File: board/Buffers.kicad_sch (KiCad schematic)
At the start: 14 parts, among them U12 74F86, U17 74F04, U52 74LS245, U53 74LS245, U54 74LS245, U55 74LS245, U56 74F541, U57 74F541

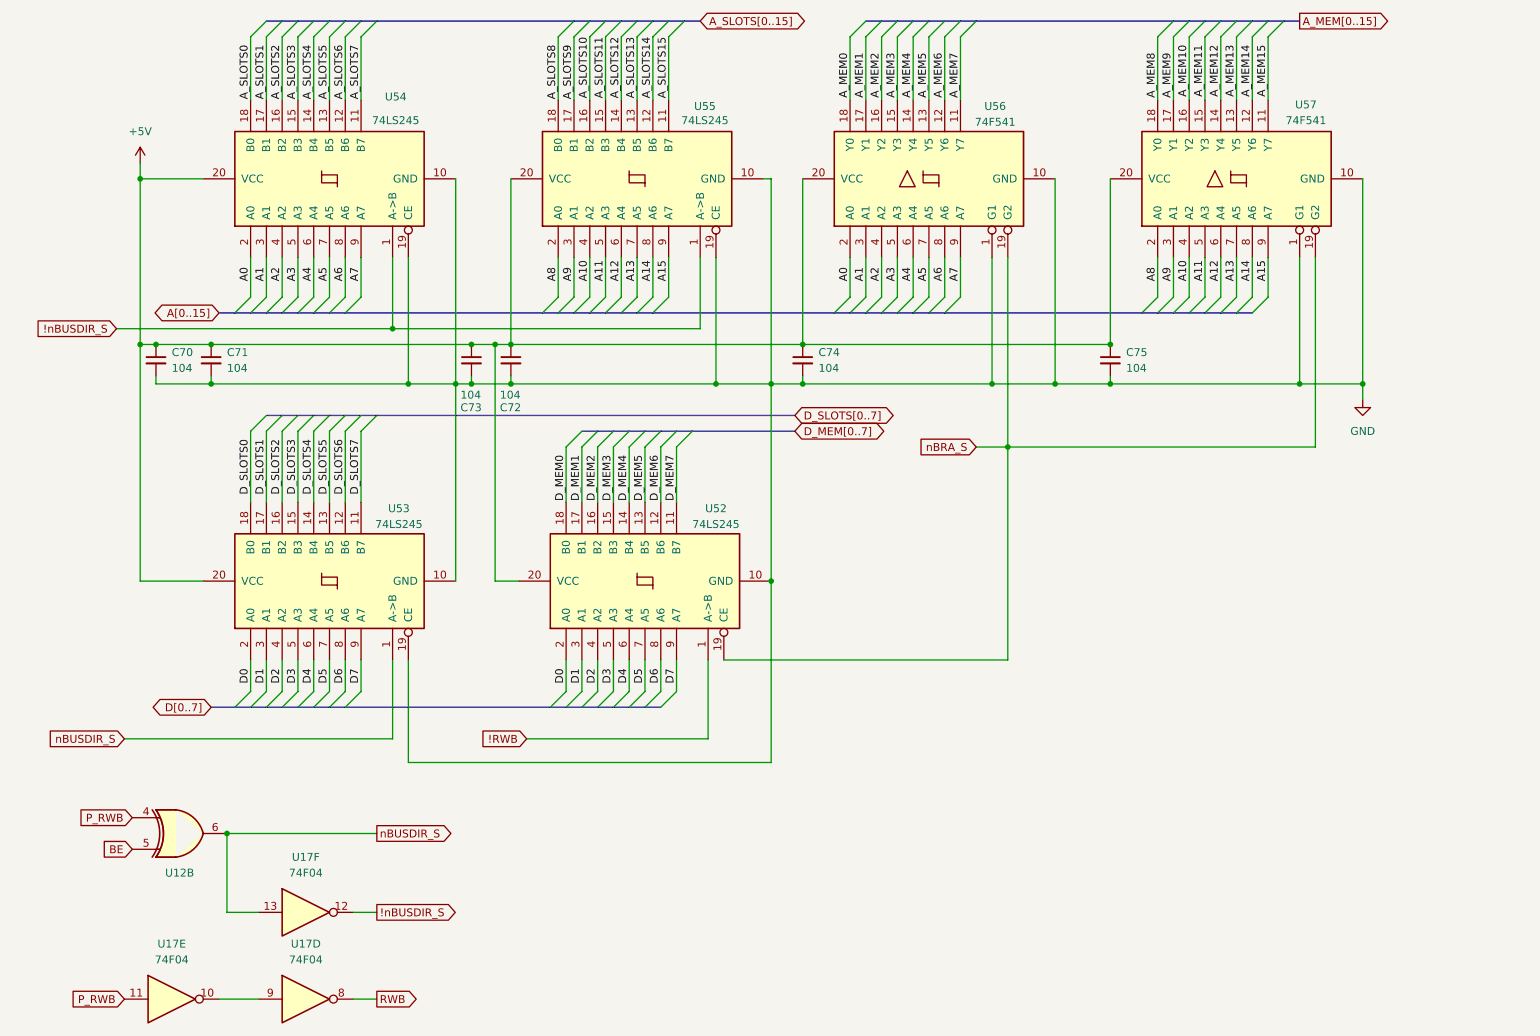
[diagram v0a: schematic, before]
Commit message: V1.3C without board traces
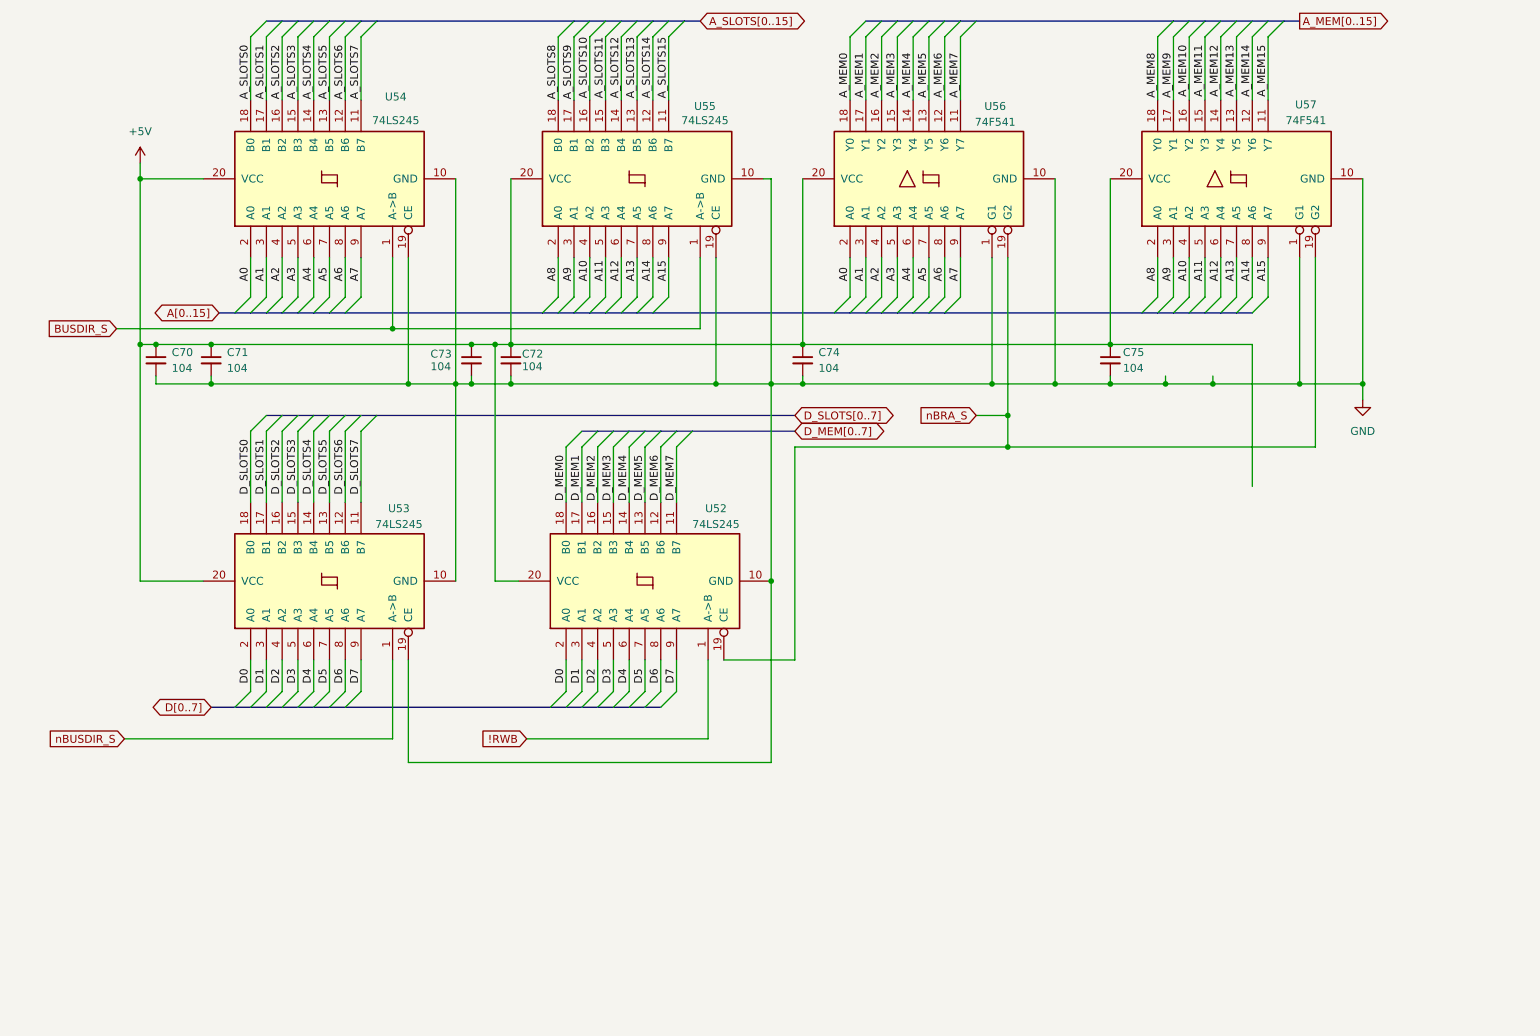
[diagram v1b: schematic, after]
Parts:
- removed U12: 74F86, Package_DIP:DIP-14_W7.62mm_Socket_LongPads, symbol 74xx:74LS86
- removed U17: 74F04, Package_DIP:DIP-14_W7.62mm_Socket_LongPads, symbol 74xx:74LS04
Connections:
- net !nBUSDIR_S renamed BUSDIR_S

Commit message: V1.4E
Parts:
- removed C72, C73, C75: 104, Capacitor_THT:C_Disc_D5.0mm_W2.5mm_P5.00mm, symbol Device:C_Small
- removed U53: 74LS245, Package_DIP:DIP-20_W7.62mm_Socket_LongPads, symbol 74xx:74LS245
- removed U56, U57: 74F541, Package_DIP:DIP-20_W7.62mm_Socket_LongPads, symbol 74xx:74LS541
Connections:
- net A_SLOTS0 is gone; now on net A0: U54.18 (B0)
- net A_SLOTS1 is gone; now on net A1: U54.17 (B1)
- net A_SLOTS10 is gone; now on net A10: U55.16 (B2)
- net A_SLOTS11 is gone; now on net A11: U55.15 (B3)
- net A_SLOTS12 is gone; now on net A12: U55.14 (B4)
- net A_SLOTS13 is gone; now on net A13: U55.13 (B5)
- net A_SLOTS14 is gone; now on net A14: U55.12 (B6)
- net A_SLOTS15 is gone; now on net A15: U55.11 (B7)
- net A_SLOTS2 is gone; now on net A2: U54.16 (B2)
- net A_SLOTS3 is gone; now on net A3: U54.15 (B3)
- net A_SLOTS4 is gone; now on net A4: U54.14 (B4)
- net A_SLOTS5 is gone; now on net A5: U54.13 (B5)
- net A_SLOTS6 is gone; now on net A6: U54.12 (B6)
- net A_SLOTS7 is gone; now on net A7: U54.11 (B7)
- net A_SLOTS8 is gone; now on net A8: U55.18 (B0)
- net A_SLOTS9 is gone; now on net A9: U55.17 (B1)
- net D_MEM0 is gone; now on net D0: U52.18 (B0)
- net D_MEM1 is gone; now on net D1: U52.17 (B1)
- net D_MEM2 is gone; now on net D2: U52.16 (B2)
- net D_MEM3 is gone; now on net D3: U52.15 (B3)
- net D_MEM4 is gone; now on net D4: U52.14 (B4)
- net D_MEM5 is gone; now on net D5: U52.13 (B5)
- net D_MEM6 is gone; now on net D6: U52.12 (B6)
- net D_MEM7 is gone; now on net D7: U52.11 (B7)
- net GND is gone; now on net nBRA_S: C70.2, C71.2, C74.2, U52.10 (GND), U54.10 (GND), U54.19 (CE), U55.10 (GND), U55.19 (CE)
- net A0: no longer U54.2 (A0)
- net A1: no longer U54.3 (A1)
- net A10: no longer U55.4 (A2)
- net A11: no longer U55.5 (A3)
- net A12: no longer U55.6 (A4)
- net A13: no longer U55.7 (A5)
- net A14: no longer U55.8 (A6)
- net A15: no longer U55.9 (A7)
- net A2: no longer U54.4 (A2)
- net A3: no longer U54.5 (A3)
- net A4: no longer U54.6 (A4)
- net A5: no longer U54.7 (A5)
- net A6: no longer U54.8 (A6)
- net A7: no longer U54.9 (A7)
- net A8: no longer U55.2 (A0)
- net A9: no longer U55.3 (A1)
- net D0: no longer U52.2 (A0)
- net D1: no longer U52.3 (A1)
- net D2: no longer U52.4 (A2)
- net D3: no longer U52.5 (A3)
- net D4: no longer U52.6 (A4)
- net D5: no longer U52.7 (A5)
- net D6: no longer U52.8 (A6)
- net D7: no longer U52.9 (A7)
- new net PA0: U54.2 (A0)
- new net PA1: U54.3 (A1)
- new net PA10: U55.4 (A2)
- new net PA11: U55.5 (A3)
- new net PA12: U55.6 (A4)
- new net PA13: U55.7 (A5)
- new net PA14: U55.8 (A6)
- new net PA15: U55.9 (A7)
- new net PA2: U54.4 (A2)
- new net PA3: U54.5 (A3)
- new net PA4: U54.6 (A4)
- new net PA5: U54.7 (A5)
- new net PA6: U54.8 (A6)
- new net PA7: U54.9 (A7)
- new net PA8: U55.2 (A0)
- new net PA9: U55.3 (A1)
- new net PD0: U52.2 (A0)
- new net PD1: U52.3 (A1)
- new net PD2: U52.4 (A2)
- new net PD3: U52.5 (A3)
- new net PD4: U52.6 (A4)
- new net PD5: U52.7 (A5)
- new net PD6: U52.8 (A6)
- new net PD7: U52.9 (A7)

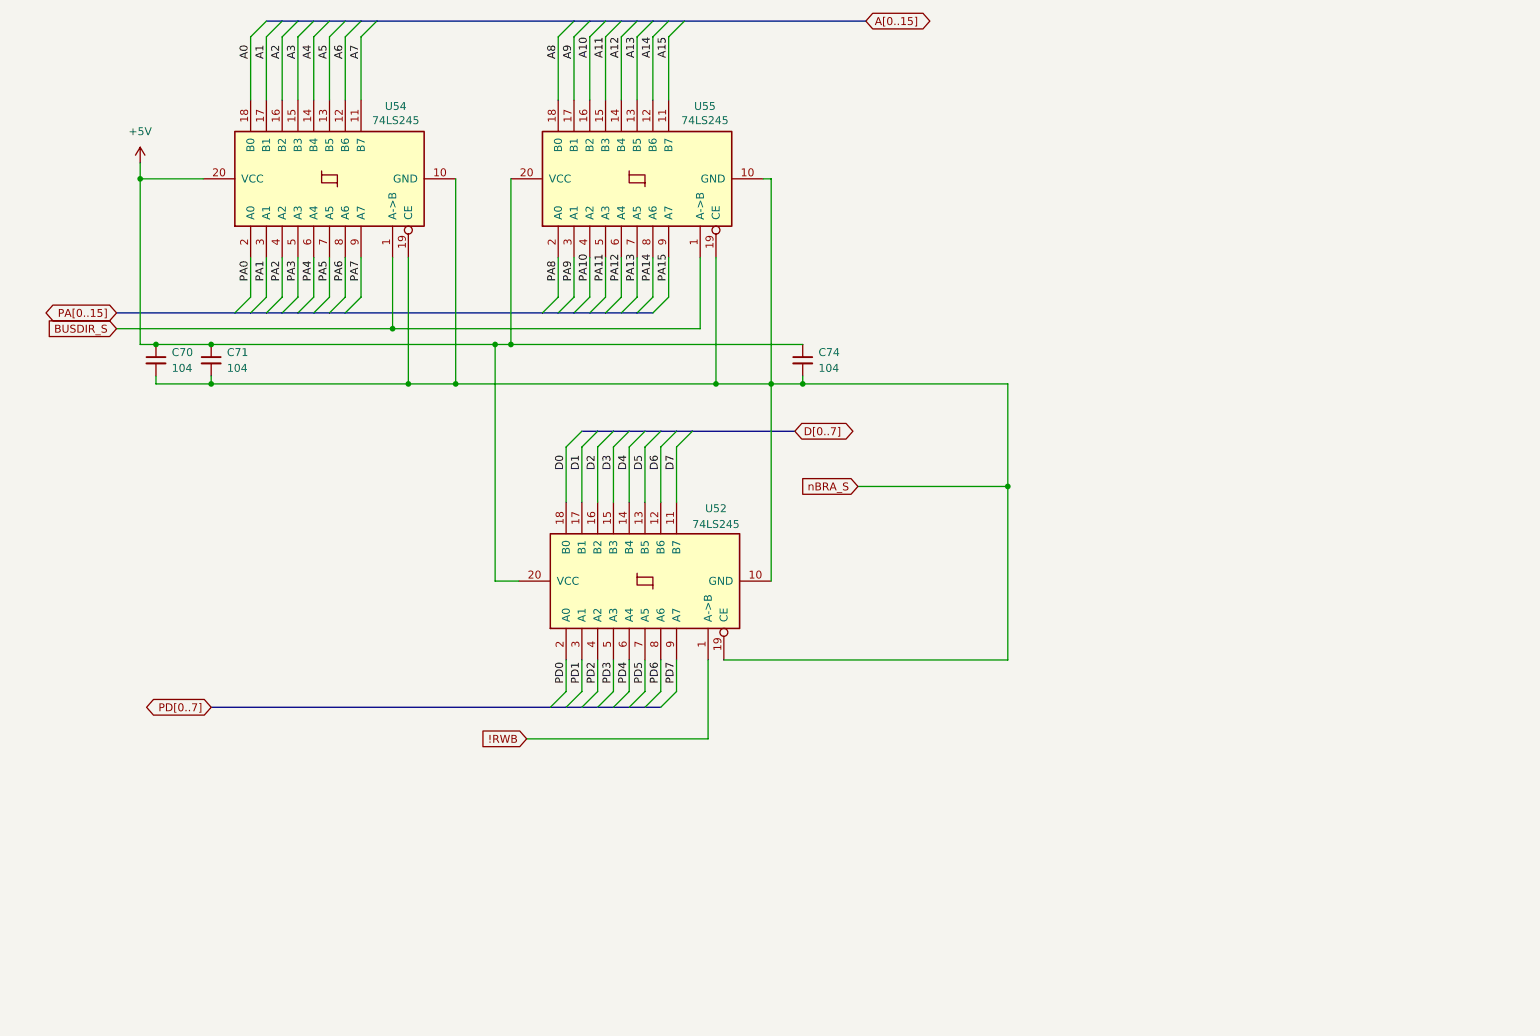
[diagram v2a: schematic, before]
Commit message: Version 1.7A: More rearrangement, partial wiring of PDB, addition of W register
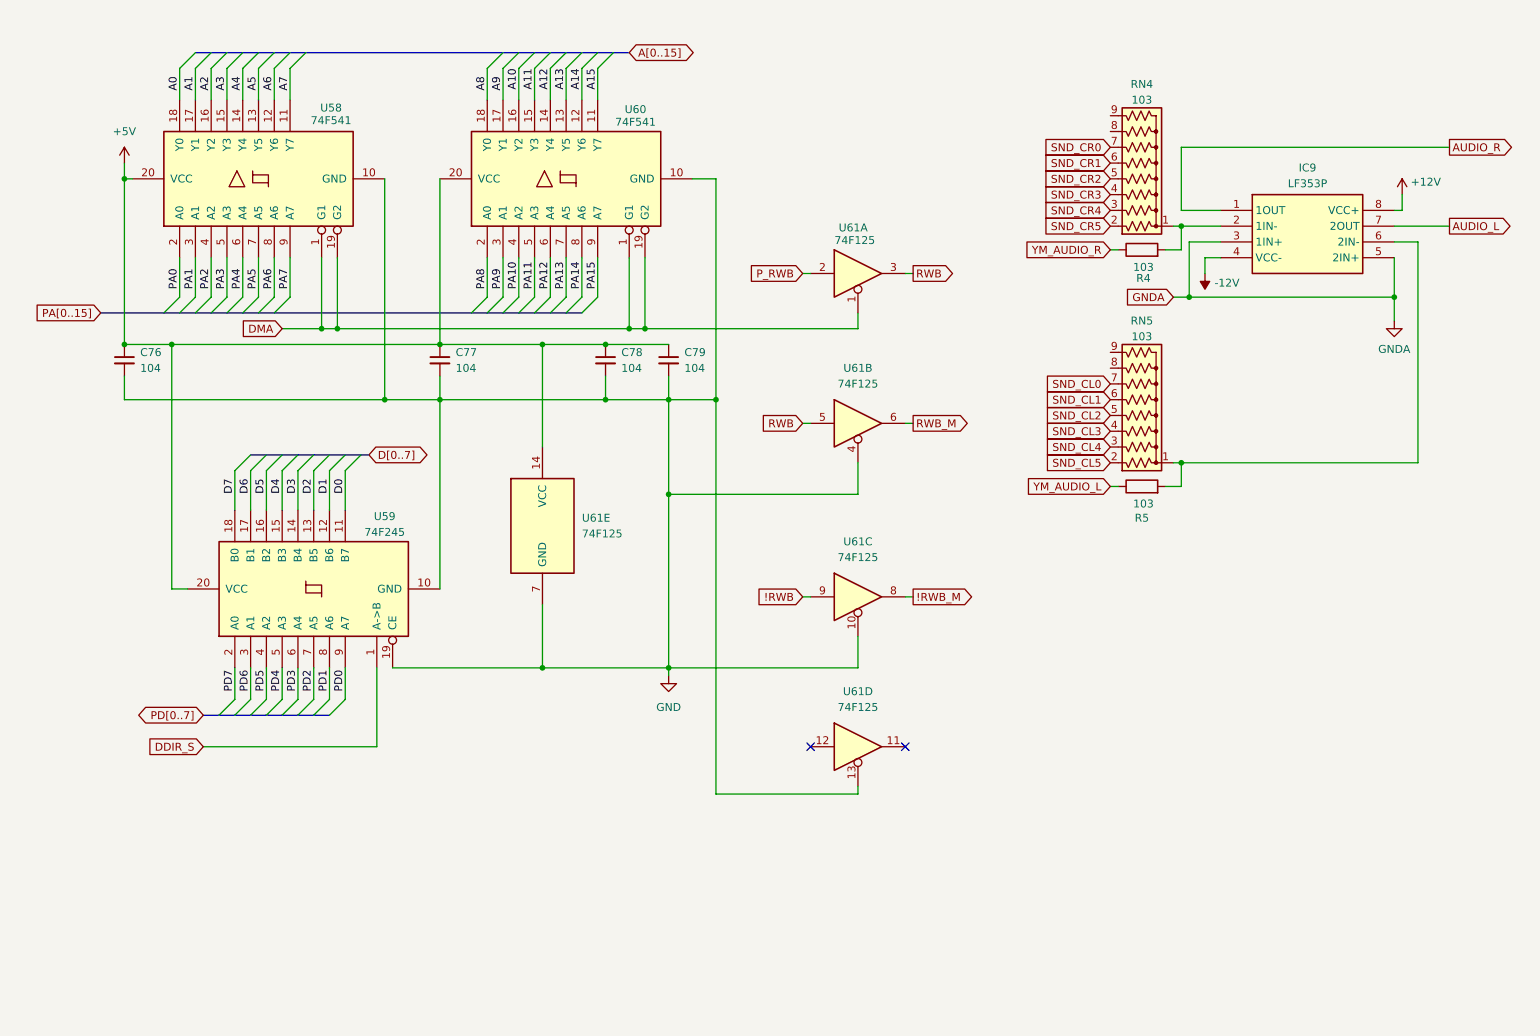
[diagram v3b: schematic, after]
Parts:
- added C79: 104, Capacitor_THT:C_Disc_D5.0mm_W2.5mm_P5.00mm, symbol Device:C_Small
- added IC9: LF353P, Package_DIP:DIP-8_W7.62mm_Socket_LongPads, symbol LF353:LF353P
- added R4, R5: 103, Resistor_THT:R_Axial_DIN0204_L3.6mm_D1.6mm_P5.08mm_Horizontal, symbol Device:R
- added RN4, RN5: 103, Resistor_THT:R_Array_SIP9, symbol Device:R_Network08_US
- added U61: 74F125, Package_DIP:DIP-14_W7.62mm_Socket_LongPads, symbol 74xx:74LS125
- U58: renamed from U54; value 74LS245 -> 74F541; symbol 74xx:74LS245 -> 74xx:74LS541
- U59: renamed from U52; value 74LS245 -> 74F245
- U60: renamed from U55; value 74LS245 -> 74F541; symbol 74xx:74LS245 -> 74xx:74LS541
- renumbered C70 to C76, C71 to C77, C74 to C78
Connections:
- net !RWB: now also U61.9; no longer U59.1 (A->B)
- net +5V: now also C79.1, U61.14 (VCC)
- net D0: now also U59.11 (B7); no longer U59.18 (B0)
- net D1: now also U59.12 (B6); no longer U59.17 (B1)
- net D2: now also U59.13 (B5); no longer U59.16 (B2)
- net D3: now also U59.14 (B4); no longer U59.15 (B3)
- net D4: now also U59.15 (B3); no longer U59.14 (B4)
- net D5: now also U59.16 (B2); no longer U59.13 (B5)
- net D6: now also U59.17 (B1); no longer U59.12 (B6)
- net D7: now also U59.18 (B0); no longer U59.11 (B7)
- net PD0: now also U59.9 (A7); no longer U59.2 (A0)
- net PD1: now also U59.8 (A6); no longer U59.3 (A1)
- net PD2: now also U59.7 (A5); no longer U59.4 (A2)
- net PD3: now also U59.6 (A4); no longer U59.5 (A3)
- net PD4: now also U59.5 (A3); no longer U59.6 (A4)
- net PD5: now also U59.4 (A2); no longer U59.7 (A5)
- net PD6: now also U59.3 (A1); no longer U59.8 (A6)
- net PD7: now also U59.2 (A0); no longer U59.9 (A7)
- net BUSDIR_S renamed DMA
- net DMA: now also U58.19 (G2), U60.19 (G2), U61.1
- net nBRA_S renamed GND
- net GND: now also C79.2, U61.10, U61.13, U61.4, U61.7 (GND); no longer U58.19 (CE), U60.19 (CE)
- new net: IC9.2 (1IN-), R4.2, RN4.1 (common)
- new net: IC9.6 (2IN-), R5.2, RN5.1 (common)
- new net !RWB_M: U61.8
- new net +12V: IC9.8 (VCC+)
- new net -12V: IC9.4 (VCC-)
- new net AUDIO_L: IC9.7 (2OUT)
- new net AUDIO_R: IC9.1 (1OUT)
- new net DDIR_S: U59.1 (A->B)
- new net GNDA: IC9.3 (1IN+), IC9.5 (2IN+)
- new net P_RWB: U61.2
- new net RWB: U61.3, U61.5
- new net RWB_M: U61.6
- new net SND_CL0: RN5.7 (R6)
- new net SND_CL1: RN5.6 (R5)
- new net SND_CL2: RN5.5 (R4)
- new net SND_CL3: RN5.4 (R3)
- new net SND_CL4: RN5.3 (R2)
- new net SND_CL5: RN5.2 (R1)
- new net SND_CR0: RN4.7 (R6)
- new net SND_CR1: RN4.6 (R5)
- new net SND_CR2: RN4.5 (R4)
- new net SND_CR3: RN4.4 (R3)
- new net SND_CR4: RN4.3 (R2)
- new net SND_CR5: RN4.2 (R1)
- new net YM_AUDIO_L: R5.1
- new net YM_AUDIO_R: R4.1
- no-connect marks 0 -> 2
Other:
- title: Buffers -> Buffers & Mixer
- moved on the sheet: C76, C77, C78, U59
